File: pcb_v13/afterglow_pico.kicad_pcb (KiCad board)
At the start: 2 copper layers, 57.5 x 57.5 mm, 52 parts, among them J1 Conn_02x17_Odd_Even, J2 Conn_02x17_Odd_Even, J3 Conn_01x02_Male, U1 74LS21, U2 7408, U3 SN74LVC245AN, U4 SN74LVC245AN, U5 Raspberry Pi Pico, U6 74LS245, U7 74LS245, U8 74LS257, U9 74LS257

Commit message: Before routing
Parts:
- BFL_LOGO, C1, C2, C3, C4, C7, C8, U1, U2, U3, U4, U6, U7: moved to F.Cu
- R1, R10, R11, R12, R13, R14, R15, R16, R2, R3, R4, R5, R6, R7, R8, R9: footprint Resistors_SMD:R_0805_HandSoldering -> pcb_v13:R_0805_HandSoldering; moved to F.Cu
- R17, R18, R19, R20, R21, R22, R23, R24, R25, R26: footprint Resistor_SMD:R_0805_2012Metric_Pad1.20x1.40mm_HandSolder -> pcb_v13:R_0805_HandSoldering; moved to F.Cu
- moved D2 79.7 mm to (172.7, 57.1), turned to 90 degrees
- moved R18 70.6 mm to (193.7, 51.3), turned to 0 degrees
- moved R1 70.3 mm to (176.5, 49.8), turned to 90 degrees
- moved R10 70.3 mm to (178.9, 49.8), turned to 90 degrees
- moved R11 70.3 mm to (174.1, 49.8), turned to -90 degrees
- moved R12 70.3 mm to (171.7, 49.8), turned to -90 degrees
- moved R13 70.3 mm to (169.3, 49.8), turned to -90 degrees
- moved R14 70.3 mm to (166.9, 49.8), turned to -90 degrees
- moved R15 70.3 mm to (164.5, 49.8), turned to -90 degrees
- moved R4 70.3 mm to (162.1, 49.8), turned to -90 degrees
- moved R6 70.3 mm to (188.5, 49.8), turned to 90 degrees
- moved R7 70.3 mm to (186.1, 49.8), turned to 90 degrees
- moved R8 70.3 mm to (183.7, 49.8), turned to 90 degrees
- moved R9 70.3 mm to (181.3, 49.8), turned to 90 degrees
- moved R17 65.1 mm to (193.7, 48.3), turned to 0 degrees
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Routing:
- net GND: track 435.4 -> 132.6 mm, vias 4 -> 0
- net +5V: track 322.8 -> 62.2 mm, vias 10 -> 0
- net /PICO_BLANK: track 143.0 -> 0.00 mm, vias 3 -> 0
- net +3V3: track 140.0 -> 0.00 mm, vias 4 -> 0
- net /PICO_EN_OUT: track 138.0 -> 0.00 mm, vias 6 -> 0
- net /P33: track 94.4 -> 0.00 mm
- net /LROW_PICO: track 88.8 -> 0.00 mm, vias 4 -> 0
- net /D5: track 88.7 -> 0.00 mm, vias 1 -> 0
- net /D6: track 82.0 -> 0.00 mm, vias 3 -> 0
- net /OUT_SEL: track 80.1 -> 0.00 mm, vias 6 -> 0
- net /DIS3: track 75.5 -> 0.00 mm, vias 2 -> 0
- net Net-(U5-Pad20): track 69.1 -> 0.00 mm, vias 1 -> 0
- net /D4_PICO: track 68.0 -> 0.00 mm, vias 1 -> 0
- net /D7_PICO: track 64.8 -> 0.00 mm, vias 3 -> 0
- net /COMB_EV: track 54.7 -> 0.00 mm
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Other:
- board size 57.5 x 57.5 mm -> 57.5 x 100 mm
- board text removed: "(c) 2021"
- board text removed: "74LS08"
- board text removed: "74LS21"
- board text removed: "74LS245"
- board text removed: "74LS257"
- board text removed: "74LVC245"
- board text removed: "Raspberry Pi Pico"
- board text removed: "v1.2 WPC"

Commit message: First PCB v1.3 draft
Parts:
- added G***: LOGO, pcb_v13:qr_code, B.Cu at (170.5, 129.9)
- + 5V -: renamed from J3
- moved BFL_LOGO 1.70 mm to (196.7, 132.3)
- renumbered PWR_LED1 to PWR, TEST_MODE1 to TEST
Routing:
- net GND: track 132.6 -> 481.6 mm, vias 0 -> 2
- net +5V: track 62.2 -> 271.4 mm, vias 0 -> 5
- net +3V3: track 0.00 -> 159.4 mm, vias 0 -> 2
- net /D2: track 0.00 -> 157.9 mm, vias 0 -> 4
- net /D1: track 0.00 -> 157.4 mm, vias 0 -> 3
- net /PICO_EN_OUT: track 0.00 -> 152.3 mm, vias 0 -> 4
- net /D3: track 0.00 -> 139.1 mm, vias 0 -> 3
- net /D4: track 0.00 -> 134.0 mm, vias 0 -> 2
- net /D7: track 0.00 -> 131.6 mm, vias 0 -> 3
- net /D6: track 0.00 -> 126.9 mm, vias 0 -> 5
- net /D0: track 0.00 -> 121.3 mm, vias 0 -> 2
- net /D5: track 0.00 -> 97.8 mm, vias 0 -> 4
- net /DIS_STROBE: track 0.00 -> 83.3 mm
- net /BLANK: track 0.00 -> 81.4 mm, vias 0 -> 1
- net /LROW: track 0.00 -> 75.2 mm, vias 0 -> 2
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- added copper zone on B.Cu, net GND
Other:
- board text added: "74LS08"
- board text added: "74LS21"
- board text added: "74LS245"
- board text added: "74LS257"
- board text added: "74LVC245"

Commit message: Routable PCB
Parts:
- C1, C2, C3, C4, C8, D2, R1, R10, R11, R12, R13, R14, R15, R16, R17, R18, R19, R2, R20, R21, R22, R23, R24, R25, R26, R3, R4, R5, R6, R7, R8, R9, U2, U3, U4, U6, U7: moved to B.Cu
- moved G*** 117.1 mm to (141.5, 16.4)
- moved U3 99.7 mm to (181.0, 30.4)
- moved C1 99.2 mm to (161.4, 25.2), turned to 180 degrees
- moved TEST 82.7 mm to (181.1, 18.4)
- moved C2 79.3 mm to (195.5, 23.1), turned to 90 degrees
- moved U5 71.8 mm to (165.7, 44.9)
- moved D1 69.2 mm to (185.2, 70.7), turned to 0 degrees
- moved R16 63.6 mm to (174.6, 17.8)
- moved R2 59.4 mm to (172.6, 26.0), turned to -90 degrees
- moved R5 56.2 mm to (195.5, 28.2), turned to 90 degrees
- moved U4 55.1 mm to (161.5, 63.2)
- moved R9 53.1 mm to (216.4, 89.7), turned to 180 degrees
- moved C6 50.9 mm to (189.3, 36.9), turned to 180 degrees
- moved U6 49.5 mm to (161.5, 33.7), turned to 0 degrees
- moved BFL_LOGO 49.3 mm to (240.9, 110.5)
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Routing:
- net GND: track 481.6 -> 55.6 mm, vias 2 -> 0
- net +5V: track 271.4 -> 51.1 mm, vias 5 -> 0
- net +3V3: track 159.4 -> 0.00 mm, vias 2 -> 0
- net /D2: track 157.9 -> 0.00 mm, vias 4 -> 0
- net /D1: track 157.4 -> 0.00 mm, vias 3 -> 0
- net /PICO_EN_OUT: track 152.3 -> 0.00 mm, vias 4 -> 0
- net /D3: track 139.1 -> 0.00 mm, vias 3 -> 0
- net /D4: track 134.0 -> 0.00 mm, vias 2 -> 0
- net /D7: track 131.6 -> 0.00 mm, vias 3 -> 0
- net /D6: track 126.9 -> 0.00 mm, vias 5 -> 0
- net /D0: track 121.3 -> 0.00 mm, vias 2 -> 0
- net /D5: track 97.8 -> 0.00 mm, vias 4 -> 0
- net /DIS_STROBE: track 83.3 -> 0.00 mm
- net /BLANK: track 81.4 -> 0.00 mm, vias 1 -> 0
- net /LROW: track 75.2 -> 0.00 mm, vias 2 -> 0
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- removed copper zone on B.Cu, net GND
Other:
- board size 57.5 x 100 mm -> 69.4 x 88.1 mm

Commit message: First attempt
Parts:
- removed AG_LOGO: LOGO, afterglow_pico:ag_pico_logo_2
- removed BFL_LOGO: LOGO, afterglow_pico:bl_logo
- added C1: 27p, Capacitor_SMD:C_0402_1005Metric, F.Cu at (147.2, 78.8)
- added C10: 100n, Capacitor_SMD:C_0402_1005Metric, F.Cu at (158.8, 75.7)
- added C11: 100n, Capacitor_SMD:C_0402_1005Metric, F.Cu at (155.2, 88.3)
- added C12: 100n, Capacitor_SMD:C_0402_1005Metric, F.Cu at (155.2, 75.6)
- added C13: 100n, Capacitor_SMD:C_0402_1005Metric, F.Cu at (149.1, 82.8)
- added C14: 100n, Capacitor_SMD:C_0402_1005Metric, F.Cu at (159.8, 88.2)
- added C15: 100n, Capacitor_SMD:C_0402_1005Metric, F.Cu at (161.2, 88.2)
- added C18: 100n, Capacitor_SMD:C_0402_1005Metric, F.Cu at (165.6, 76.3)
- added C2: 27p, Capacitor_SMD:C_0402_1005Metric, F.Cu at (147.2, 81.8)
- added C3: 100n, Capacitor_SMD:C_0402_1005Metric, F.Cu at (164.2, 80.4)
- added C4: 10u, Capacitor_SMD:C_0805_2012Metric, F.Cu at (191.0, 138.3)
- added C5: 100n, Capacitor_SMD:C_0402_1005Metric, F.Cu at (149.1, 83.8)
- added C6: 1u, Capacitor_SMD:C_0402_1005Metric, F.Cu at (162.8, 84.3)
- added C7: 10u, Capacitor_SMD:C_0805_2012Metric, F.Cu at (200.6, 133.9)
- added C8: 100n, Capacitor_SMD:C_0402_1005Metric, F.Cu at (164.2, 81.3)
- added C9: 1u, Capacitor_SMD:C_0402_1005Metric, F.Cu at (162.8, 85.3)
- added D2: BAT60A, Diode_SMD:D_SOD-323, F.Cu at (193.6, 142.4)
- added D4: WS2812B, LED_SMD:LED_WS2812B_PLCC4_5.0x5.0mm_P3.2mm, F.Cu at (142.2, 63.2)
- added J1: USB_B_Micro, Connector_USB:USB_Micro-B_Molex-105017-0001, F.Cu at (168.2, 61.0)
- added J3: Conn_01x02, Connector_PinHeader_2.54mm:PinHeader_1x02_P2.54mm_Vertical, F.Cu at (152.7, 62.1)
- added R1: 1k, Resistor_SMD:R_0402_1005Metric, F.Cu at (149.1, 81.1)
- added R14: 10k, Resistor_SMD:R_0402_1005Metric, F.Cu at (158.9, 73.3)
- added R2: 27, Resistor_SMD:R_0402_1005Metric, F.Cu at (162.8, 82.3)
- added R3: 27, Resistor_SMD:R_0402_1005Metric, F.Cu at (162.8, 83.3)
- added R32: 4.7k, Resistor_SMD:R_0402_1005Metric, F.Cu at (200.2, 118.9)
- added R33: 4.7k, Resistor_SMD:R_0402_1005Metric, F.Cu at (200.2, 114.1)
- added R34: 4.7k, Resistor_SMD:R_0402_1005Metric, F.Cu at (200.2, 121.3)
- added R35: 4.7k, Resistor_SMD:R_0402_1005Metric, F.Cu at (200.2, 116.5)
- added R36: 4.7k, Resistor_SMD:R_0402_1005Metric, F.Cu at (200.2, 111.7)
- added R6: 1k, Resistor_SMD:R_0402_1005Metric, F.Cu at (156.1, 62.2)
- added U1: NCP1117-3.3_SOT223, Package_TO_SOT_SMD:SOT-223-3_TabPin2, F.Cu at (199.3, 140.7)
- added U2: RP2040, RP2040_minimal:RP2040-QFN-56, F.Cu at (156.2, 82.3)
- added Y1: ABLS-12.000MHZ-B4-T, RP2040_minimal:Crystal_SMD_HC49-US, F.Cu at (143.1, 80.2)
- C16: renamed from C1; footprint Capacitors_SMD:C_0805_HandSoldering -> Capacitor_SMD:C_0402_1005Metric; moved to F.Cu
- C17: renamed from C2; footprint Capacitors_SMD:C_0805_HandSoldering -> Capacitor_SMD:C_0402_1005Metric; moved to F.Cu
- C19: renamed from C7; footprint Capacitors_SMD:C_0805_HandSoldering -> Capacitor_SMD:C_0402_1005Metric
- C20: renamed from C3; footprint Capacitors_SMD:C_0805_HandSoldering -> Capacitor_SMD:C_0402_1005Metric; moved to F.Cu
- C21: renamed from C4; footprint Capacitors_SMD:C_0805_HandSoldering -> Capacitor_SMD:C_0402_1005Metric; moved to F.Cu
- C22: renamed from C5; footprint Capacitors_SMD:C_0805_HandSoldering -> Capacitor_SMD:C_0402_1005Metric
- C23: renamed from C6; footprint Capacitors_SMD:C_0805_HandSoldering -> Capacitor_SMD:C_0402_1005Metric
- C24: renamed from C8; footprint Capacitors_SMD:C_0805_HandSoldering -> Capacitor_SMD:C_0402_1005Metric; moved to F.Cu
- D3: renamed from D2; moved to F.Cu
- J2: renamed from + 5V -
- PWR_LED1: renamed from PWR; footprint LEDs:LED_0805_HandSoldering -> LED_SMD:LED_0402_1005Metric
- R10: renamed from R22; footprint pcb_v13:R_0805_HandSoldering -> Resistor_SMD:R_0402_1005Metric; moved to F.Cu
- R11: renamed from R23; footprint pcb_v13:R_0805_HandSoldering -> Resistor_SMD:R_0402_1005Metric; moved to F.Cu
- R12: renamed from R24; footprint pcb_v13:R_0805_HandSoldering -> Resistor_SMD:R_0402_1005Metric; moved to F.Cu
- R13: renamed from R25; footprint pcb_v13:R_0805_HandSoldering -> Resistor_SMD:R_0402_1005Metric; moved to F.Cu
- R15: renamed from R26; footprint pcb_v13:R_0805_HandSoldering -> Resistor_SMD:R_0402_1005Metric; moved to F.Cu
- R16: renamed from R2; footprint pcb_v13:R_0805_HandSoldering -> Resistor_SMD:R_0402_1005Metric; moved to F.Cu
- R17: renamed from R6; footprint pcb_v13:R_0805_HandSoldering -> Resistor_SMD:R_0402_1005Metric; moved to F.Cu
- R18: renamed from R7; footprint pcb_v13:R_0805_HandSoldering -> Resistor_SMD:R_0402_1005Metric; moved to F.Cu
- R19: renamed from R8; footprint pcb_v13:R_0805_HandSoldering -> Resistor_SMD:R_0402_1005Metric; moved to F.Cu
- R20: renamed from R9; footprint pcb_v13:R_0805_HandSoldering -> Resistor_SMD:R_0402_1005Metric; moved to F.Cu
- R21: renamed from R10; footprint pcb_v13:R_0805_HandSoldering -> Resistor_SMD:R_0402_1005Metric; moved to F.Cu
- R22: renamed from R11; footprint pcb_v13:R_0805_HandSoldering -> Resistor_SMD:R_0402_1005Metric; moved to F.Cu
- R23: renamed from R12; footprint pcb_v13:R_0805_HandSoldering -> Resistor_SMD:R_0402_1005Metric; moved to F.Cu
- R24: renamed from R13; footprint pcb_v13:R_0805_HandSoldering -> Resistor_SMD:R_0402_1005Metric; moved to F.Cu
- R25: renamed from R14; footprint pcb_v13:R_0805_HandSoldering -> Resistor_SMD:R_0402_1005Metric; moved to F.Cu
- R26: renamed from R15; footprint pcb_v13:R_0805_HandSoldering -> Resistor_SMD:R_0402_1005Metric; moved to F.Cu
- R27: renamed from R5; footprint pcb_v13:R_0805_HandSoldering -> Resistor_SMD:R_0402_1005Metric; moved to F.Cu
- R28: renamed from R16; footprint pcb_v13:R_0805_HandSoldering -> Resistor_SMD:R_0402_1005Metric; moved to F.Cu
- R29: renamed from R3; footprint pcb_v13:R_0805_HandSoldering -> Resistor_SMD:R_0402_1005Metric; moved to F.Cu
- R30: renamed from R4; footprint pcb_v13:R_0805_HandSoldering -> Resistor_SMD:R_0402_1005Metric; moved to F.Cu
- R31: renamed from R1; footprint pcb_v13:R_0805_HandSoldering -> Resistor_SMD:R_0402_1005Metric; moved to F.Cu
- R4: renamed from R17; footprint pcb_v13:R_0805_HandSoldering -> Resistor_SMD:R_0402_1005Metric; moved to F.Cu
- R5: renamed from R18; footprint pcb_v13:R_0805_HandSoldering -> Resistor_SMD:R_0402_1005Metric; moved to F.Cu
- R7: renamed from R19; footprint pcb_v13:R_0805_HandSoldering -> Resistor_SMD:R_0402_1005Metric; moved to F.Cu
- R8: renamed from R20; footprint pcb_v13:R_0805_HandSoldering -> Resistor_SMD:R_0402_1005Metric; moved to F.Cu
- R9: renamed from R21; footprint pcb_v13:R_0805_HandSoldering -> Resistor_SMD:R_0402_1005Metric; moved to F.Cu
- U10: renamed from U8; value 74LS257 -> 74HC257; footprint Housings_SSOP:SOP-16_4.4x10.4mm_Pitch1.27mm -> Package_SO:TSSOP-16_4.4x5mm_P0.65mm
- U11: renamed from U9; value 74LS257 -> 74HC257; footprint Housings_SSOP:SOP-16_4.4x10.4mm_Pitch1.27mm -> Package_SO:TSSOP-16_4.4x5mm_P0.65mm
- U3, U4: footprint Housings_SOIC:SOIC-20W_7.5x12.8mm_Pitch1.27mm -> Package_SO:TSSOP-20_4.4x6.5mm_P0.65mm; moved to F.Cu
- U5: value Raspberry Pi Pico -> W25Q32JVSS; footprint SnapEDA Library:MODULE_SC0915 -> Package_SO:SOIC-8_5.23x5.23mm_P1.27mm
- U6: renamed from U1; value 74LS21 -> 74HC21
- U7: renamed from U2; moved to F.Cu
- U8: renamed from U6; value 74LS245 -> 74HC245; footprint Housings_SOIC:SOIC-20W_7.5x12.8mm_Pitch1.27mm -> Package_SO:TSSOP-20_4.4x6.5mm_P0.65mm; moved to F.Cu
- U9: renamed from U7; value 74LS245 -> 74HC245; footprint Housings_SOIC:SOIC-20W_7.5x12.8mm_Pitch1.27mm -> Package_SO:TSSOP-20_4.4x6.5mm_P0.65mm; moved to F.Cu
- moved D3 104.1 mm to (193.6, 138.3)
- moved C22 102.7 mm to (146.2, 113.8), turned to 0 degrees
- moved U10 93.1 mm to (145.9, 110.2)
- moved C23 83.0 mm to (158.0, 113.7), turned to 0 degrees
- moved R27 82.8 mm to (153.2, 99.3)
- moved R28 77.8 mm to (157.8, 93.8), turned to -90 degrees
- moved R22 77.2 mm to (169.3, 104.9)
- moved G*** 76.4 mm to (211.6, 46.7)
- moved D1 71.9 mm to (190.9, 142.4), turned to 90 degrees
- moved U11 71.6 mm to (158.1, 110.2)
- moved R23 69.2 mm to (170.8, 104.8)
- moved R21 67.9 mm to (168.9, 101.1)
- moved U8 67.4 mm to (145.8, 99.2), turned to -90 degrees
- moved U7 65.9 mm to (172.8, 110.9)
- moved C16 64.7 mm to (177.2, 88.0), turned to 0 degrees
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- renumbered J1 to J4, J2 to J5, TEST to TEST_MODE1
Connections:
- C20 pad 2: +5V -> Vcc
- C21 pad 1: +5V -> Vcc
- C22 pad 1: +5V -> Vcc
- C23 pad 1: +5V -> Vcc
- D1 pad 1: Net-(D1-Pad1) -> Net-(C4-Pad1)
- D1 pad 2: +5V -> VBUS
- R10 pad 1: +5V -> Vcc
- R11 pad 1: +5V -> Vcc
- R12 pad 1: +5V -> Vcc
- R13 pad 1: +5V -> Vcc
- R15 pad 1: +5V -> Vcc
- R16 pad 2: Net-(R2-Pad2) -> /GPIO11
- R22 pad 1: +5V -> Vcc
- R23 pad 1: +5V -> Vcc
- R24 pad 1: +5V -> Vcc
- R25 pad 1: +5V -> Vcc
- R26 pad 1: +5V -> Vcc
- R27 pad 1: /PICO_EN_OUT -> /GPIO13
- R28 pad 2: Net-(R16-Pad2) -> /GPIO14
- R4 pad 1: +5V -> Vcc
- R5 pad 1: +5V -> Vcc
- R7 pad 1: +5V -> Vcc
- R8 pad 1: +5V -> Vcc
- R9 pad 1: +5V -> Vcc
- TEST_MODE1 pad 1: Net-(TEST_MODE1-Pad1) -> /GPIO12
- U10 pad 15: /PICO_EN_OUT -> /GPIO13
- U10 pad 16: +5V -> Vcc
- U11 pad 15: /PICO_EN_OUT -> /GPIO13
- U11 pad 16: +5V -> Vcc
- U3 pad 11: Net-(U3-Pad11) -> /GPIO7
- U3 pad 12: Net-(U3-Pad12) -> /GPIO6
- U3 pad 13: Net-(U3-Pad13) -> /GPIO5
- U3 pad 14: Net-(U3-Pad14) -> /GPIO4
- U3 pad 15: Net-(U3-Pad15) -> /GPIO3
- U3 pad 16: Net-(U3-Pad16) -> /GPIO2
- U3 pad 17: Net-(U3-Pad17) -> /GPIO1
- U3 pad 18: Net-(U3-Pad18) -> /GPIO0
- U3 pad 19: /PICO_EN_OUT -> /GPIO13
- U4 pad 15: Net-(R2-Pad2) -> /GPIO11
- U4 pad 16: Net-(U4-Pad16) -> /GPIO10
- U4 pad 17: Net-(U4-Pad17) -> /GPIO9
- U4 pad 18: Net-(U4-Pad18) -> /GPIO8
- U4 pad 19: /PICO_EN_OUT -> /GPIO13
- U5 pad 1: Net-(U3-Pad18) -> /QSPI_SS
- U5 pad 2: Net-(U3-Pad17) -> /QSPI_SD1
- U5 pad 3: GND -> /QSPI_SD2
- U5 pad 4: Net-(U3-Pad16) -> GND
- U5 pad 5: Net-(U3-Pad15) -> /QSPI_SD0
- U5 pad 6: Net-(U3-Pad14) -> /QSPI_SCLK
- U5 pad 7: Net-(U3-Pad13) -> /QSPI_SD3
- U5 pad 8: GND -> +3V3
- U8 pad 1: +5V -> Vcc
- U8 pad 19: /PICO_EN_OUT -> /GPIO13
- U8 pad 2: Net-(U5-Pad20) -> /GPIO15
- U8 pad 20: +5V -> Vcc
- U8 pad 3: Net-(U5-Pad21) -> /GPIO16
- U8 pad 4: Net-(U5-Pad22) -> /GPIO17
- U8 pad 5: Net-(U5-Pad24) -> /GPIO18
- U8 pad 6: Net-(U5-Pad25) -> /GPIO19
- U8 pad 7: Net-(U5-Pad26) -> /GPIO20
- U8 pad 8: Net-(U5-Pad27) -> /GPIO21
- U8 pad 9: Net-(U5-Pad29) -> /GPIO22
- U9 pad 1: +5V -> Vcc
- U9 pad 14: unconnected-(U7-Pad14) -> /PICO_WS2812
- U9 pad 19: /PICO_EN_OUT -> /GPIO13
- U9 pad 2: Net-(U5-Pad31) -> /GPIO26_ADC0
- U9 pad 20: +5V -> Vcc
- U9 pad 3: Net-(U5-Pad32) -> /GPIO27_ADC1
- U9 pad 4: Net-(U5-Pad34) -> /GPIO28_ADC2
- U9 pad 5: Net-(R16-Pad2) -> /GPIO14
- U9 pad 6: GND -> /GPIO23
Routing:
- net GND: track 55.6 -> 1.03 mm
- net +5V: track 51.1 -> 0.00 mm
- net Net-(D1-Pad1): track 30.0 -> 0.00 mm
- net /USB_D-: track 0.00 -> 25.4 mm
- net +3V3: track 0.00 -> 24.6 mm
- net /USB_D+: track 0.00 -> 23.8 mm
- net /QSPI_SS: track 0.00 -> 21.4 mm
- net /QSPI_SD1: track 0.00 -> 20.0 mm
- net /QSPI_SD2: track 0.00 -> 15.7 mm
- net /XIN: track 0.00 -> 14.4 mm
- net +1V1: track 0.00 -> 11.1 mm
- net /QSPI_SD3: track 0.00 -> 10.5 mm
- net Net-(C2-Pad1): track 0.00 -> 9.65 mm
- net /QSPI_SCLK: track 0.00 -> 9.51 mm
- net /QSPI_SD0: track 0.00 -> 8.41 mm
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- added copper zone on F.Cu, net +1V1
- added copper zone on F.Cu, net +3V3
- added copper zone on F.Cu, net GND
- added copper zone on In1.Cu, net GND
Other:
- outline, holes or cut-outs redrawn
- copper layers 2 -> 4
- board text removed: "74LS08"
- board text removed: "74LS21"
- board text removed: "74LS245"
- board text removed: "74LS257"
- board text removed: "74LVC245"

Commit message: Placement
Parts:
- moved C16 8.28 mm to (179.1, 79.9), turned to 180 degrees
- moved R28 5.41 mm to (152.8, 95.5), turned to 90 degrees
- moved C22 2.71 mm to (143.6, 113.0)
- moved U8 2.46 mm to (143.6, 98.0)
- moved U10 2.45 mm to (143.6, 109.3)
- moved C20 2.42 mm to (147.9, 98.0)
- moved U4 2.32 mm to (179.1, 71.7)
- moved C17 2.10 mm to (179.1, 76.2)
- moved U3 2.05 mm to (179.1, 84.1), turned to 0 degrees
- moved R16 1.95 mm to (173.4, 71.3)
- moved R26 1.43 mm to (176.9, 104.7)
- moved C21 1.39 mm to (161.5, 98.0)
- moved U9 1.28 mm to (157.2, 98.0)
- moved U11 1.26 mm to (157.2, 109.3)
- moved C23 1.10 mm to (157.2, 113.0)
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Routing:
- net +5V: track 0.00 -> 13.1 mm
- net +3V3: track 24.6 -> 36.6 mm
- net Net-(C4-Pad1): track 0.00 -> 5.44 mm
- net GND: track 1.03 -> 3.06 mm, vias 0 -> 1

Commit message: Power routing
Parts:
- moved D3 5.21 mm to (190.8, 142.7), turned to 90 degrees
- moved C4 4.98 mm to (193.4, 142.7), turned to -90 degrees
- moved D2 4.68 mm to (190.8, 138.7), turned to -90 degrees
- moved D1 4.49 mm to (193.4, 138.7)
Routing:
- net Vcc: track 0.00 -> 305.0 mm, vias 0 -> 21
- net +3V3: track 36.6 -> 181.1 mm, vias 0 -> 9
- net VBUS: track 0.00 -> 107.1 mm, vias 0 -> 2
- net GND: track 3.06 -> 45.3 mm, vias 1 -> 25
- net Net-(C4-Pad1): track 5.44 -> 8.78 mm
- net +5V: track 13.1 -> 10.2 mm

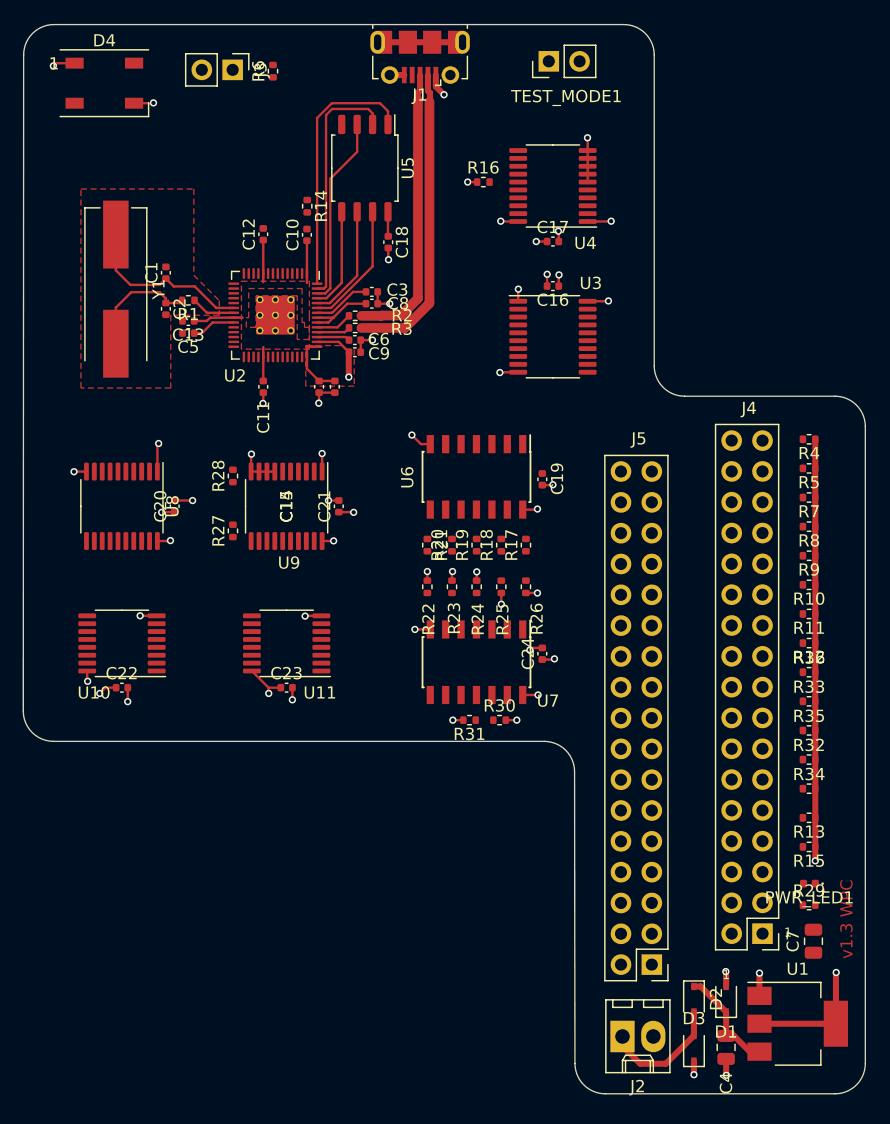
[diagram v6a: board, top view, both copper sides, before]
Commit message: Power routing
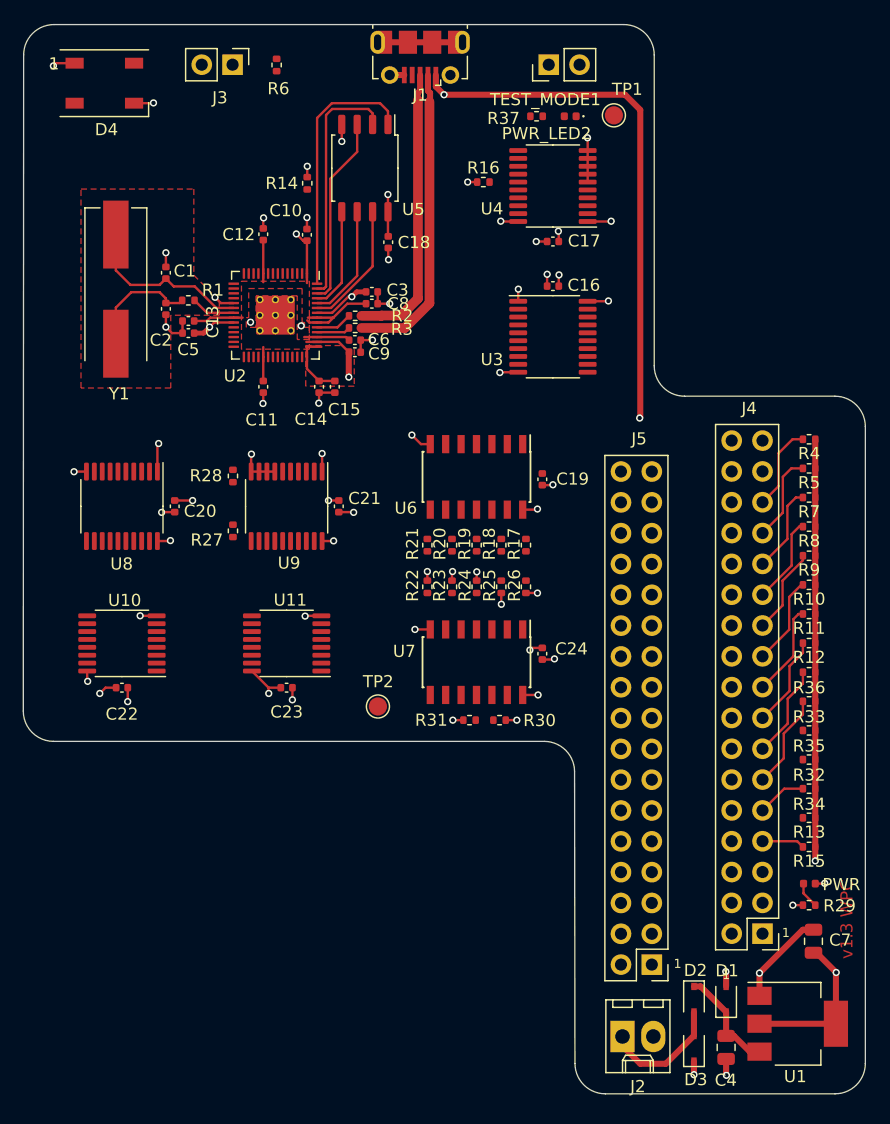
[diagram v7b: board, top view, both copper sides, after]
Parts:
- added PWR_LED2: LED, LED_SMD:LED_0402_1005Metric, F.Cu at (180.6, 65.9)
- added R37: 1k, Resistor_SMD:R_0402_1005Metric, F.Cu at (177.8, 65.9)
- added TP1: TestPoint, TestPoint:TestPoint_Pad_D1.5mm, F.Cu at (184.2, 65.8)
- added TP2: TestPoint, TestPoint:TestPoint_Pad_D1.5mm, F.Cu at (164.7, 114.5)
- moved G*** 60.6 mm to (160.1, 78.5)
- moved R14 1.89 mm to (158.9, 71.4)
- moved R6 0.59 mm to (156.3, 61.7)
- moved J3 0.43 mm to (152.7, 61.6)
- moved TEST_MODE1 0.28 mm to (178.8, 61.6)
- renumbered PWR_LED1 to PWR
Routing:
- net +3V3: track 181.1 -> 211.1 mm, vias 9 -> 13
- net GND: track 45.3 -> 61.7 mm, vias 25 -> 32
- net VBUS: track 107.1 -> 95.3 mm, vias 2 -> 3
- net +1V1: track 11.1 -> 20.9 mm, vias 0 -> 4
- net /SOL3: track 0.00 -> 7.83 mm
- net /TRIAC: track 0.00 -> 7.69 mm
- net /D6: track 0.00 -> 7.62 mm
- net /D7: track 0.00 -> 7.55 mm
- net /D5: track 0.00 -> 7.35 mm
- net /D1: track 0.00 -> 7.27 mm
- net /D2: track 0.00 -> 7.19 mm
- net /D3: track 0.00 -> 7.17 mm
- net /D4: track 0.00 -> 7.13 mm
- net /D0: track 0.00 -> 7.07 mm
- net /SOL2: track 0.00 -> 4.07 mm
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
